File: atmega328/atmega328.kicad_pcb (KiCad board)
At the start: 2 copper layers, 35.6 x 48.3 mm, 25 parts, among them J1 INPUT, J2 FTDI, J3 ISP-2560, J4 DIGOUT1, J5 DIGOUT2, U1 NCP1117-5V, U2 ATMEGA328, X1 16MHz 18pF

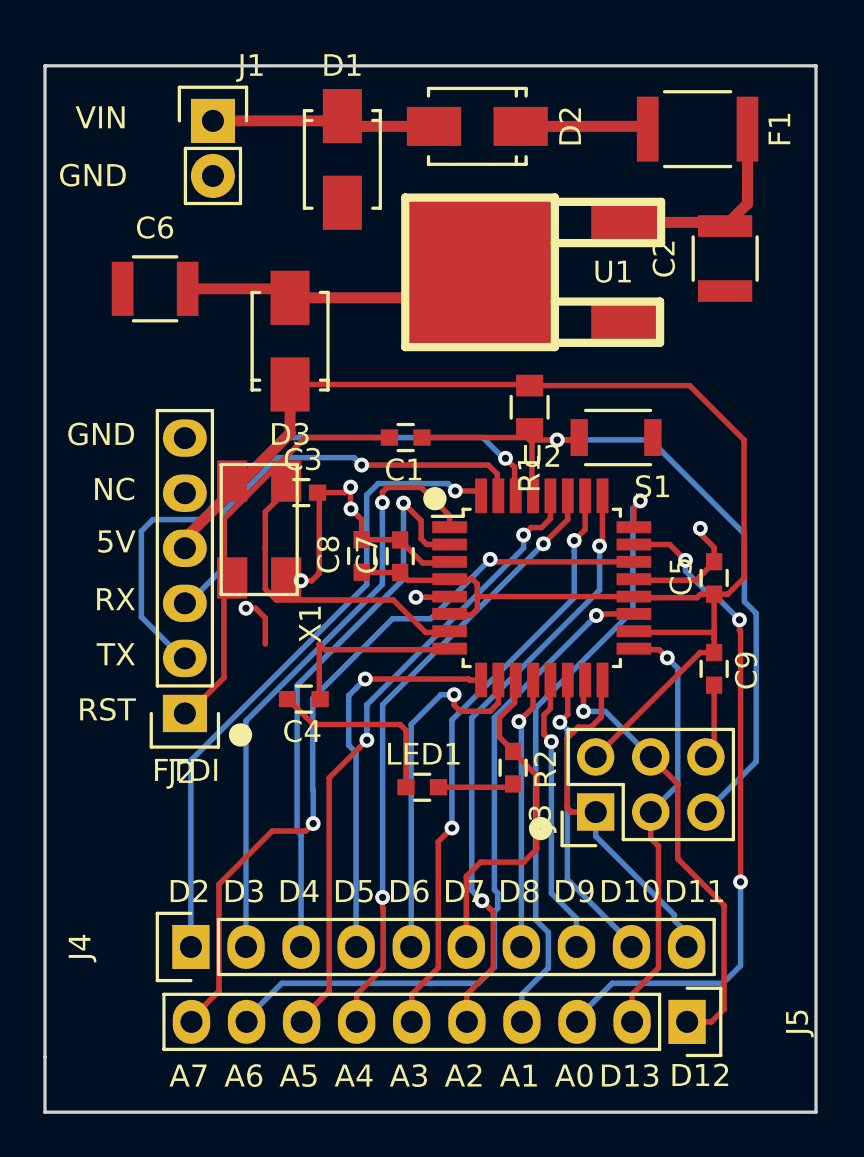
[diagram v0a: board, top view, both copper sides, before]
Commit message: File got screwed up when footprints were adjusted, fixed it up. Gerbers reflect the actual board.
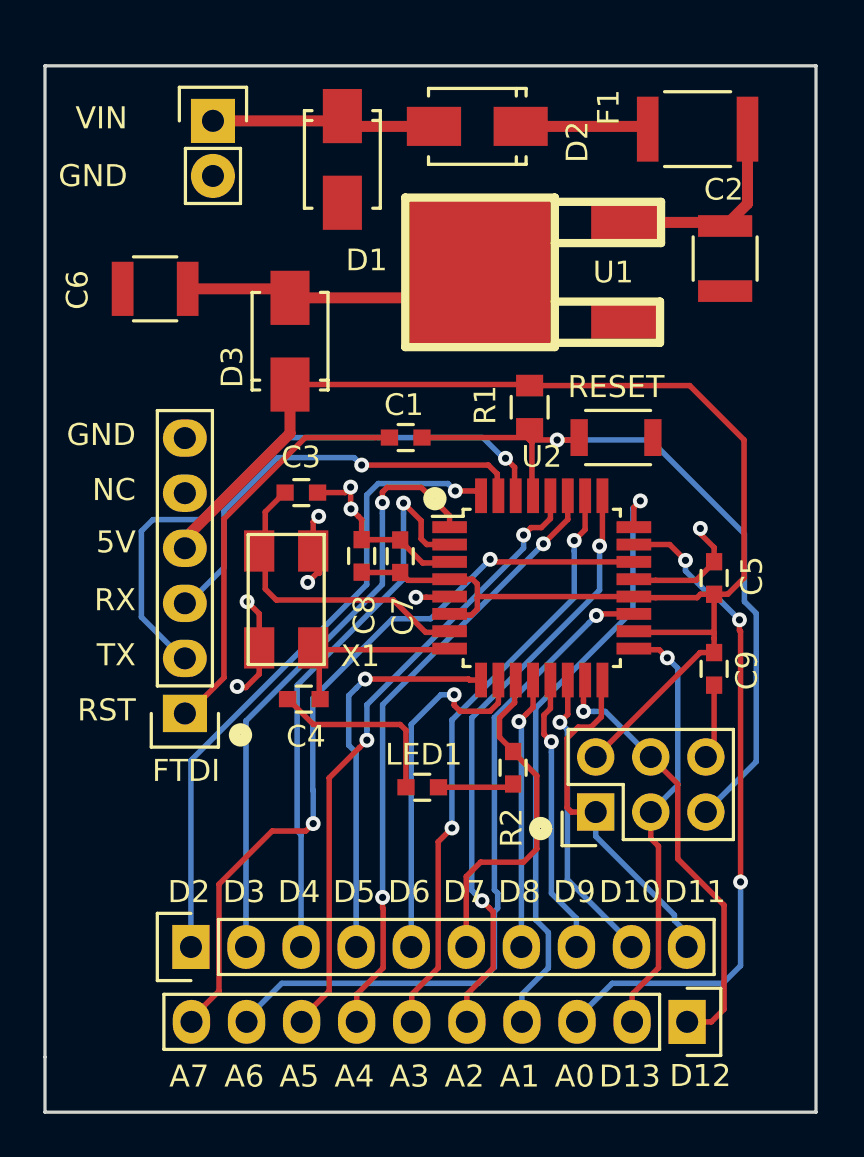
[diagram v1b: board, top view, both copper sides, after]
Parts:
- moved X1 3.46 mm to (116.4, 111.8)
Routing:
- net GND: track 32.1 -> 36.9 mm, vias 4 -> 8
- net (no net): track 2.28 -> 0.00 mm, vias 1 -> 0
- net Net-(C4-Pad1): track 9.60 -> 8.62 mm, vias 1 -> 0
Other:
- board text added: "RESET"

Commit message: Added Atmega328 v1.1 to fix Tx/Rx and add breakout pins.
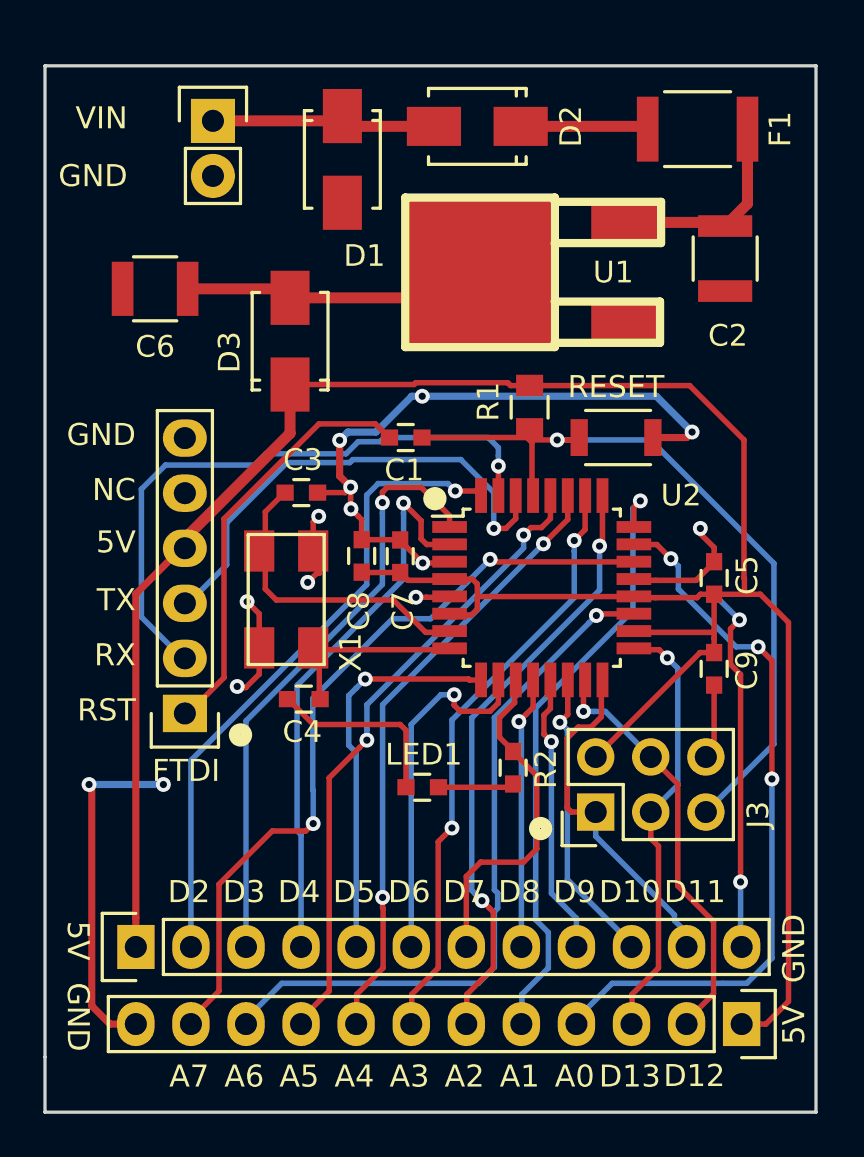
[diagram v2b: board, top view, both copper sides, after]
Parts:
- C1, C3, C4, C5, C7, C8, C9, LED1: footprint Wickerlib:0603 -> Wickerlib:RLC-0603-SMD
- C2, C6: footprint Wickerlib:1210 -> Wickerlib:RLC-1210-SMD
- D1, D2, D3: footprint Wickerlib:Diode_SMA -> Wickerlib:DIODE-SMA
- F1: footprint Wickerlib:1812 -> Wickerlib:RLC-1812-SMD
- J1: footprint Wickerlib:OSTVN02A150 -> Wickerlib:CONN-ONSHORE-SCREW-GREEN-2PIN-TH
- J2: footprint Wickerlib:Pin_Header_Straight_1x06 -> Wickerlib:CONN-HEADER-STRAIGHT-P2.54MM-1x06
- J3: footprint Wickerlib:Pin_Header_Straight_2x03 -> Wickerlib:CONN-HEADER-STRAIGHT-P2.54MM-2x03
- J4: value DIGOUT1 -> HEADER-FEMALE-12POS-TH-1x12-P0.1IN; footprint Wickerlib:Pin_Header_Straight_1x10 -> Wickerlib:CONN-HEADER-STRAIGHT-P2.54MM-1x12
- J5: value DIGOUT2 -> HEADER-FEMALE-12POS-TH-1x12-P0.1IN; footprint Wickerlib:Pin_Header_Straight_1x10 -> Wickerlib:CONN-HEADER-STRAIGHT-P2.54MM-1x12
- R1: footprint Wickerlib:0805 -> Wickerlib:RLC-0805-SMD
- R2: value 1K -> 220; footprint Wickerlib:0603 -> Wickerlib:RLC-0603-SMD
- S1: footprint Wickerlib:SW-B3U-1000P -> Wickerlib:SWITCH-OMRON-MOMENTARY-SMD-B3U-1000P
- U2: value ATMEGA328 -> IC-MCU-ATMEGA328-TQFP32-CUSTOM1; footprint Wickerlib:TQFP-32_7x7mm_Pitch0.8mm -> Wickerlib:TQFP-32-7x7MM-P0.8MM
- moved J4 2.54 mm to (109.7, 127.8)
- moved J5 2.52 mm to (137.7, 131.3)
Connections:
- J2 pad 2: /D0 -> /FTDI_RX/D1_TX
- J2 pad 3: /D1 -> /FTDI_TX/D0_RX
- J4 pad 1: /D2 -> +5V
- J4 pad 10: /D11 -> /D10
- J4 pad 2: /D3 -> /D2
- J4 pad 3: /D4 -> /D3
- J4 pad 4: /D5 -> /D4
- J4 pad 5: /D6 -> /D5
- J4 pad 6: /D7 -> /D6
- J4 pad 7: /D8 -> /D7
- J4 pad 8: /D9 -> /D8
- J4 pad 9: /D10 -> /D9
- J5 pad 1: /D12 -> +5V
- J5 pad 10: /A7(*) -> /A6(*)
- J5 pad 2: /D13 -> /D12
- J5 pad 3: /A0 -> /D13
- J5 pad 4: /A1 -> /A0
- J5 pad 5: /A2 -> /A1
- J5 pad 6: /A3 -> /A2
- J5 pad 7: /A4 -> /A3
- J5 pad 8: /A5 -> /A4
- J5 pad 9: /A6(*) -> /A5
- U2 pad 30: /D0 -> /FTDI_TX/D0_RX
- U2 pad 31: /D1 -> /FTDI_RX/D1_TX
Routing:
- net GND: track 36.9 -> 92.9 mm, vias 8 -> 16
- net +5V: track 73.5 -> 116.1 mm
- net /FTDI_RX/D1_TX: track 0.00 -> 28.6 mm, vias 0 -> 1
- net /D0: track 27.7 -> 0.00 mm, vias 1 -> 0
- net /FTDI_TX/D0_RX: track 0.00 -> 23.0 mm, vias 0 -> 1
- net /D1: track 20.2 -> 0.00 mm, vias 1 -> 0
- net /A0: track 31.3 -> 33.2 mm
- net /D12: track 20.4 -> 19.4 mm
- net /~RESET: track 35.0 -> 35.6 mm
- net /FTDI_RESET: track 19.0 -> 19.5 mm
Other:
- net class Default: clearance 0.254 -> 0.1524
- rule pad_to_mask_clearance: 0.2 -> 0.0762
- rule trace_clearance: 0.254 -> 0.1524
- board text added: "9/21/16"
- board text added: "Atmega328 Breakout Board v1.1"
- board text added: "Atmega328 Breakout v1.1"
- board text removed: "Atmega328 Breakout v1.0"

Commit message: Created new atmega328 project folder.
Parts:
- removed C1, C5, C7, C8, C9: 100nF, Wickerlib:RLC-0603-SMD
- removed C2, C6: 10uF 25V, Wickerlib:RLC-1210-SMD
- removed C3, C4: 22pF, Wickerlib:RLC-0603-SMD
- removed D1: 14V, Wickerlib:DIODE-SMA
- removed D2, D3: 20V 1A, Wickerlib:DIODE-SMA
- removed F1: 1.1A 25V, Wickerlib:RLC-1812-SMD
- removed J1: INPUT, Wickerlib:CONN-ONSHORE-SCREW-GREEN-2PIN-TH
- removed J2: FTDI, Wickerlib:CONN-HEADER-STRAIGHT-P2.54MM-1x06
- removed J3: ISP-2560, Wickerlib:CONN-HEADER-STRAIGHT-P2.54MM-2x03
- removed J4, J5: HEADER-FEMALE-12POS-TH-1x12-P0.1IN, Wickerlib:CONN-HEADER-STRAIGHT-P2.54MM-1x12
- removed LED1: AMBER, Wickerlib:RLC-0603-SMD
- removed R1: 10K, Wickerlib:RLC-0805-SMD
- removed R2: 220, Wickerlib:RLC-0603-SMD
- removed S1: RESET, Wickerlib:SWITCH-OMRON-MOMENTARY-SMD-B3U-1000P
- removed U1: NCP1117-5V, Wickerlib:DPAK
- removed U2: IC-MCU-ATMEGA328-TQFP32-CUSTOM1, Wickerlib:TQFP-32-7x7MM-P0.8MM
- removed X1: 16MHz 18pF, Wickerlib:CRYSTAL-CTS-4SMD
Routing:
- net +5V: track 116.1 -> 0.00 mm
- net GND: track 92.9 -> 0.00 mm, vias 16 -> 0
- net /A7(*): track 35.7 -> 0.00 mm, vias 2 -> 0
- net /~RESET: track 35.6 -> 0.00 mm, vias 1 -> 0
- net /A0: track 33.2 -> 0.00 mm, vias 3 -> 0
- net /A6(*): track 32.6 -> 0.00 mm, vias 1 -> 0
- net /D2: track 29.9 -> 0.00 mm, vias 1 -> 0
- net /A5: track 29.3 -> 0.00 mm, vias 2 -> 0
- net /FTDI_RX/D1_TX: track 28.6 -> 0.00 mm, vias 1 -> 0
- net /A4: track 28.3 -> 0.00 mm, vias 2 -> 0
- net /A1: track 28.1 -> 0.00 mm, vias 1 -> 0
- net /D3: track 27.8 -> 0.00 mm, vias 1 -> 0
- net /A2: track 27.7 -> 0.00 mm, vias 2 -> 0
- net /A3: track 27.6 -> 0.00 mm, vias 2 -> 0
- net /D4: track 26.0 -> 0.00 mm, vias 1 -> 0
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- removed copper zone on B.Cu, net GND
- removed copper zone on F.Cu, net GND
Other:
- board outline removed
- net class Default: clearance 0.1524 -> 0.254
- rule trace_clearance: 0.1524 -> 0.254
- board text removed: "5V"
- board text removed: "9/21/16"
- board text removed: "A0"
- board text removed: "A1"
- board text removed: "A2"
- board text removed: "A3"
- board text removed: "A4"
- board text removed: "A5"
- board text removed: "A6"
- board text removed: "A7"
- board text removed: "Atmega328 Breakout Board v1.1"
- board text removed: "Atmega328 Breakout v1.1"
- board text removed: "D10"
- board text removed: "D11"
- board text removed: "D12"
- board text removed: "D13"
- board text removed: "D2"
- board text removed: "D3"
- board text removed: "D4"
- board text removed: "D5"
- board text removed: "D6"
- board text removed: "D7"
- board text removed: "D8"
- board text removed: "D9"
- board text removed: "FTDI"
- board text removed: "GND"
- board text removed: "NC"
- board text removed: "RESET"
- board text removed: "RST"
- board text removed: "RX"
- board text removed: "TX"
- board text removed: "VIN"
- board text removed: "wickerbox.net/wickerlib"

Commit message: Converted atmega328 to new project format.
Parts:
- added C1: 100nF, Wickerlib:RLC-0603-SMD, F.Cu at (122.2, 104.3)
- added C2: 10uF 25V, Wickerlib:RLC-1210-SMD, F.Cu at (136.9, 96.0)
- added C3: 22pF, Wickerlib:RLC-0603-SMD, F.Cu at (117.4, 106.8)
- added C4: 22pF, Wickerlib:RLC-0603-SMD, F.Cu at (117.5, 116.3)
- added C5: 100nF, Wickerlib:RLC-0603-SMD, F.Cu at (136.4, 110.7)
- added C6: 10uF 25V, Wickerlib:RLC-1210-SMD, F.Cu at (110.6, 97.4)
- added C7: 100nF, Wickerlib:RLC-0603-SMD, F.Cu at (121.9, 109.7)
- added C8: 100nF, Wickerlib:RLC-0603-SMD, F.Cu at (120.1, 109.7)
- added C9: 100nF, Wickerlib:RLC-0603-SMD, F.Cu at (136.4, 114.9)
- added D1: 14V, Wickerlib:DIODE-SMA, F.Cu at (119.3, 91.4)
- added D2: 20V 1A, Wickerlib:DIODE-SMA, F.Cu at (125.5, 89.9)
- added D3: 20V 1A, Wickerlib:DIODE-SMA, F.Cu at (116.8, 99.8)
- added F1: 1.1A 25V, Wickerlib:RLC-1812-SMD, F.Cu at (135.6, 90.0)
- added J1: INPUT, Wickerlib:CONN-ONSHORE-SCREW-GREEN-2PIN-TH, F.Cu at (113.3, 89.7)
- added J2: FTDI, Wickerlib:CONN-HEADER-STRAIGHT-P2.54MM-1x06, F.Cu at (112.0, 117.0)
- added J3: ISP-2560, Wickerlib:CONN-HEADER-STRAIGHT-P2.54MM-2x03, F.Cu at (130.9, 121.5)
- added J4: HEADER-FEMALE-12POS-TH-1x12-P0.1IN, Wickerlib:CONN-HEADER-STRAIGHT-P2.54MM-1x12, F.Cu at (109.7, 127.8)
- added J5: HEADER-FEMALE-12POS-TH-1x12-P0.1IN, Wickerlib:CONN-HEADER-STRAIGHT-P2.54MM-1x12, F.Cu at (137.7, 131.3)
- added LED1: AMBER, Wickerlib:RLC-0603-SMD, F.Cu at (122.9, 120.4)
- added R1: 10K, Wickerlib:RLC-0805-SMD, F.Cu at (127.9, 102.9)
- added R2: 220, Wickerlib:RLC-0603-SMD, F.Cu at (127.1, 119.5)
- added S1: RESET, Wickerlib:SWITCH-OMRON-MOMENTARY-SMD-B3U-1000P, F.Cu at (133.6, 104.3)
- added U1: NCP1117-5V, Wickerlib:DPAK, F.Cu at (132.3, 96.6)
- added U2: IC-MCU-ATMEGA328-TQFP32-CUSTOM1, Wickerlib:TQFP-32-7x7MM-P0.8MM, F.Cu at (128.4, 111.2)
- added X1: 16MHz 18pF, Wickerlib:CRYSTAL-CTS-4SMD, F.Cu at (116.4, 111.8)
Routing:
- net +5V: track 0.00 -> 116.1 mm
- net GND: track 0.00 -> 92.9 mm, vias 0 -> 16
- net /A7(*): track 0.00 -> 35.7 mm, vias 0 -> 2
- net /~RESET: track 0.00 -> 35.6 mm, vias 0 -> 1
- net /A0: track 0.00 -> 33.2 mm, vias 0 -> 3
- net /A6(*): track 0.00 -> 32.6 mm, vias 0 -> 1
- net /D2: track 0.00 -> 29.9 mm, vias 0 -> 1
- net /A5: track 0.00 -> 29.3 mm, vias 0 -> 2
- net /FTDI_RX/D1_TX: track 0.00 -> 28.6 mm, vias 0 -> 1
- net /A4: track 0.00 -> 28.3 mm, vias 0 -> 2
- net /A1: track 0.00 -> 28.1 mm, vias 0 -> 1
- net /D3: track 0.00 -> 27.8 mm, vias 0 -> 1
- net /A2: track 0.00 -> 27.7 mm, vias 0 -> 2
- net /A3: track 0.00 -> 27.6 mm, vias 0 -> 2
- net /D4: track 0.00 -> 26.0 mm, vias 0 -> 1
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- added copper zone on B.Cu, net GND
- added copper zone on F.Cu, net GND
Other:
- board outline added: 35.6 x 48.3 mm
- net class Default: clearance 0.254 -> 0.1524
- board text added: "5V"
- board text added: "9/21/16"
- board text added: "A0"
- board text added: "A1"
- board text added: "A2"
- board text added: "A3"
- board text added: "A4"
- board text added: "A5"
- board text added: "A6"
- board text added: "A7"
- board text added: "Atmega328 Breakout Board v1.1"
- board text added: "Atmega328 Breakout v1.1"
- board text added: "D10"
- board text added: "D11"
- board text added: "D12"
- board text added: "D13"
- board text added: "D2"
- board text added: "D3"
- board text added: "D4"
- board text added: "D5"
- board text added: "D6"
- board text added: "D7"
- board text added: "D8"
- board text added: "D9"
- board text added: "FTDI"
- board text added: "GND"
- board text added: "NC"
- board text added: "RESET"
- board text added: "RST"
- board text added: "RX"
- board text added: "TX"
- board text added: "VIN"
- board text added: "wickerbox.net/wickerlib"

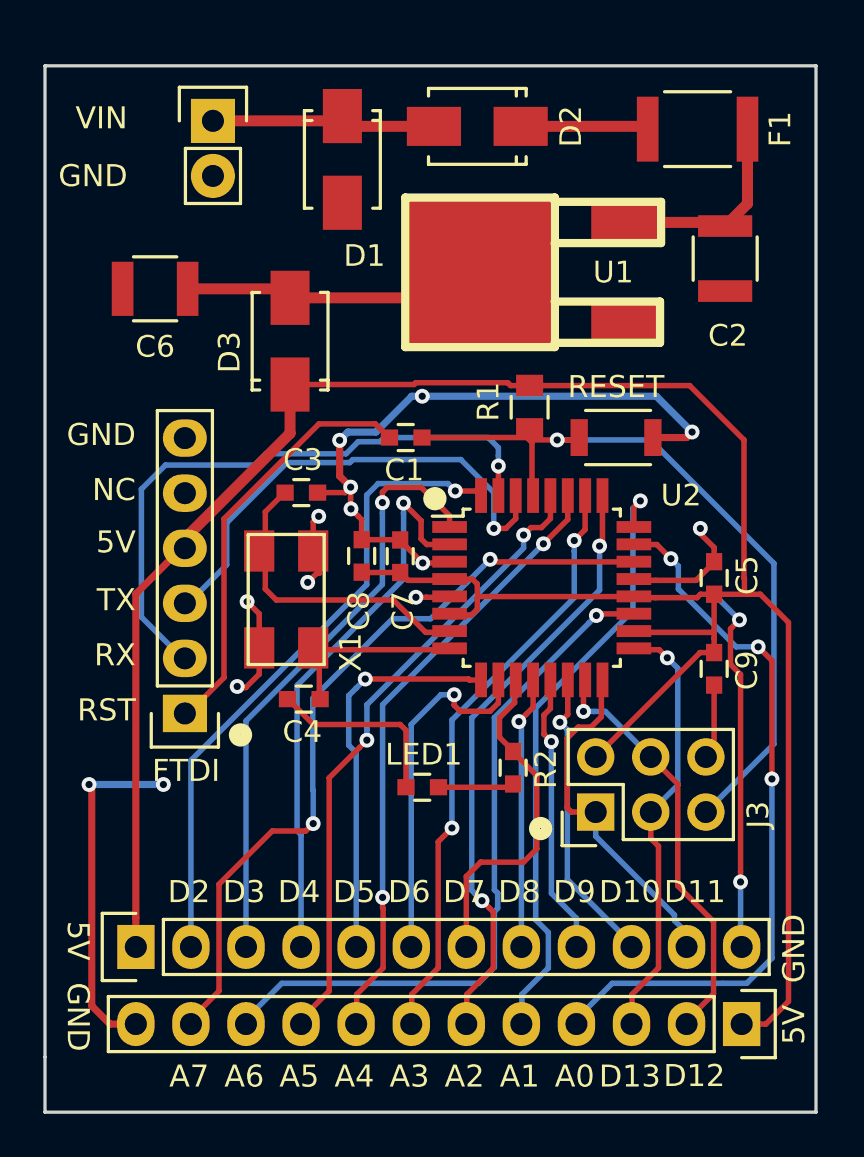
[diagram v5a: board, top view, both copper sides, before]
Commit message: Added shunt jumper.
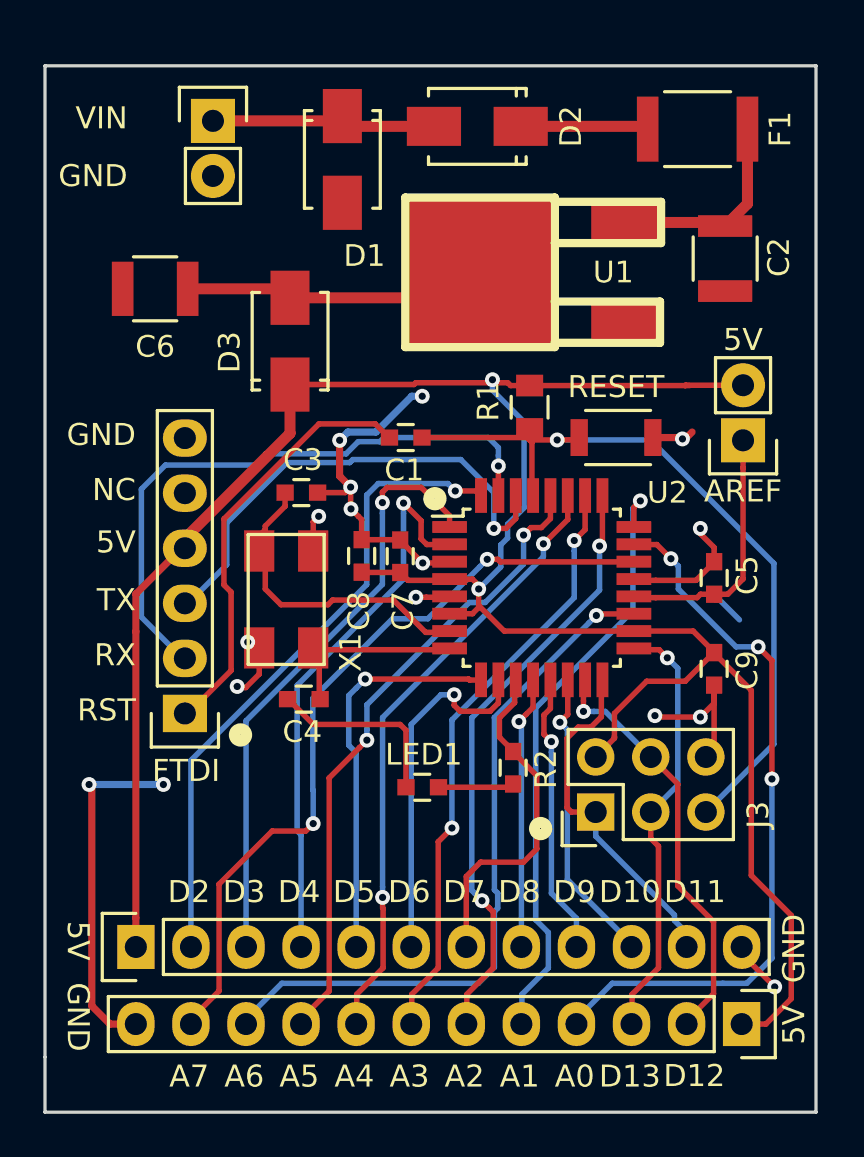
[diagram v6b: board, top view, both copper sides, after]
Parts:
- added JP1: JUMP, Wickerlib:CONN-HEADER-STRAIGHT-P2.54MM-1x02, F.Cu at (137.7, 104.4)
- U2: value IC-MCU-ATMEGA328-TQFP32-CUSTOM1 -> ATMEGA328
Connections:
- C5 pad 1: +5V -> /AREF
- U2 pad 20: +5V -> /AREF
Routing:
- net GND: track 92.9 -> 65.0 mm
- net /AREF: track 0.00 -> 11.8 mm
- net +5V: track 116.1 -> 110.5 mm, vias 0 -> 2
- net (no net): track 0.00 -> 1.56 mm
- net Net-(C3-Pad1): track 14.1 -> 15.4 mm
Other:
- rule trace_clearance: 0.254 -> 0.1524
- board text added: "12/31/16"
- board text added: "AREF"
- board text added: "Atmega328 Breakout Board v1.2"
- board text removed: "9/21/16"
- board text removed: "Atmega328 Breakout Board v1.1"

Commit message: New gerbers, had to fix version silk.
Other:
- board text added: "Atmega328 Breakout v1.2"
- board text added: "wickerbox.net"
- board text removed: "Atmega328 Breakout v1.1"
- board text removed: "wickerbox.net/wickerlib"
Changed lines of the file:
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@@
     (effects (font (size 1.016 1.016) (thickness 0.2032)) (justify right))
   )
-  (gr_text wickerbox.net/wickerlib (at 107.569 100.2284 90) (layer B.SilkS)
+  (gr_text "wickerbox.net\n\n" (at 108.331 94.9325 90) (layer B.SilkS)
     (effects (font (size 1.27 1.27) (thickness 0.254)) (justify mirror))
   )
-  (gr_text "Atmega328 \nBreakout\nv1.1" (at 138.3538 92.7608) (layer B.SilkS)
+  (gr_text "Atmega328 \nBreakout\nv1.2" (at 138.3538 92.7608) (layer B.SilkS)
     (effects (font (size 1.5 1.5) (thickness 0.3)) (justify left mirror))
   )
